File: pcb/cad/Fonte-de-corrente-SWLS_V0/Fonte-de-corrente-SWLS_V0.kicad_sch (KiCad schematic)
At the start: 31 parts, among them J2 LEMO FFA.0S, J3 LEMO FFA.0S, J4 Barrel_Jack_Switch, SW1 SW_DIP_x01, U1 LM7805, U2 LT3080xST, U3 LT3092xST, U4 LT3092xST, U5 74AHC1G04, U6 TS5A21366, U7 TS5A21366, U8 TS5A21366, U9 TS5A21366

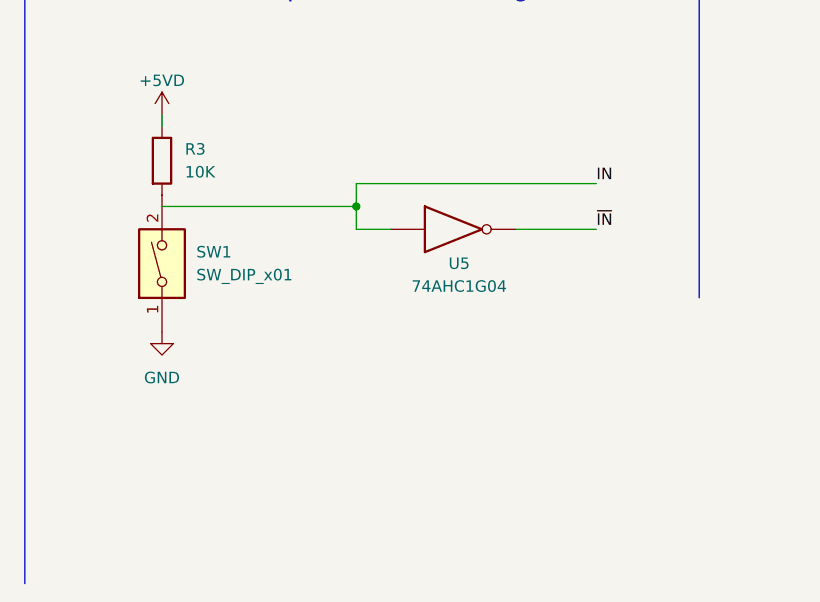
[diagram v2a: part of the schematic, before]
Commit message: Atualização do circuito esquemático, adição de footprints nod componentes
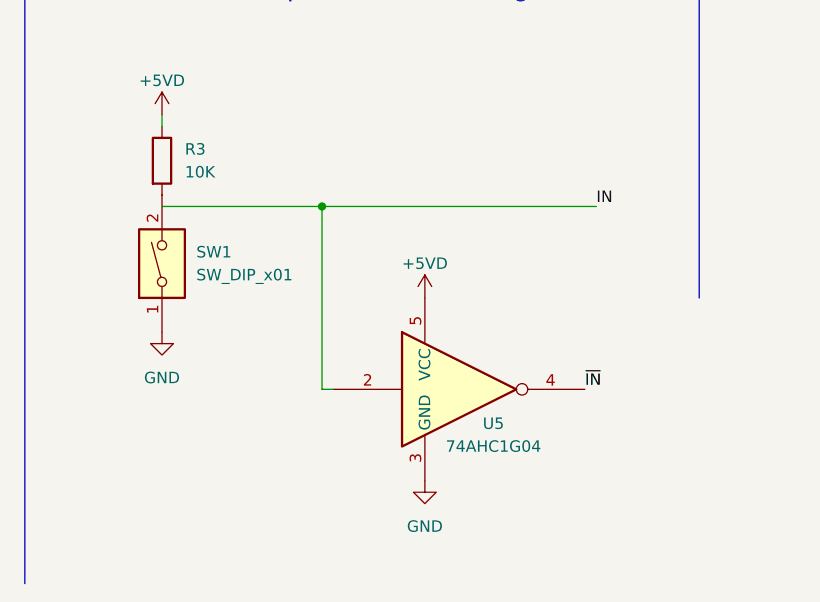
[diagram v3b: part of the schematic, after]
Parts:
- SW1: footprint (none) -> Button_Switch_THT:SW_DIP_SPSTx01_Piano_10.8x4.1mm_W7.62mm_P2.54mm; Numero do Produto (none) -> 418117270901
- U1: footprint (none) -> Package_TO_SOT_THT:TO-220-3_Vertical; Numero do produto (none) -> LM7805
- U5: footprint (none) -> Package_TO_SOT_SMD:SOT-353_SC-70-5_Handsoldering; Numero do produto (none) -> 74AHC1G04SE
- U6, U7, U8, U9: footprint (none) -> Package_SO:VSSOP-8_2.4x2.1mm_P0.5mm; Numero do produto (none) -> TS5A21366
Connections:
- net VCC is gone; now on net +5V: U5.5 (VCC)
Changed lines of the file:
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@@
   (junction (at 46.99 176.53) (diameter 0) (color 0 0 0 0)
   )
-  (junction (at 138.43 156.21) (diameter 0) (color 0 0 0 0)
-  )
   (junction (at 59.69 176.53) (diameter 0) (color 0 0 0 0)
   )
@@
   (junction (at 50.8 49.53) (diameter 0) (color 0 0 0 0)
   )
+  (junction (at 134.62 156.21) (diameter 0) (color 0 0 0 0)
+  )
   (junction (at 151.13 46.99) (diameter 0) (color 0 0 0 0)
   )
   (junction (at 46.99 46.99) (diameter 0) (color 0 0 0 0)
   )
-  (wire (pts (xy 138.43 158.75) (xy 142.24 158.75))
+  (wire (pts (xy 134.62 176.53) (xy 135.89 176.53))
     (stroke (width 0) (type default))
   )
@@
     (stroke (width 0) (type default))
   )
-  (wire (pts (xy 138.43 153.67) (xy 138.43 156.21))
-    (stroke (width 0) (type default))
-  )
   (wire (pts (xy 55.88 149.86) (xy 66.04 149.86))
     (stroke (width 0) (type default))
@@
     (stroke (width 0) (type default))
   )
-  (wire (pts (xy 116.84 156.21) (xy 138.43 156.21))
+  (wire (pts (xy 116.84 156.21) (xy 134.62 156.21))
     (stroke (width 0) (type default))
   )
@@
     (stroke (width 0) (type default))
   )
-  (wire (pts (xy 156.21 158.75) (xy 165.1 158.75))
-    (stroke (width 0) (type default))
-  )
   (wire (pts (xy 69.85 87.63) (xy 72.39 87.63))
     (stroke (width 0) (type default))
   )
-  (wire (pts (xy 138.43 153.67) (xy 165.1 153.67))
+  (wire (pts (xy 134.62 156.21) (xy 165.1 156.21))
     (stroke (width 0) (type default))
   )
@@
     (stroke (width 0) (type default))
   )
-  (wire (pts (xy 138.43 156.21) (xy 138.43 158.75))
+  (wire (pts (xy 134.62 156.21) (xy 134.62 176.53))
     (stroke (width 0) (type default))
   )
@@
     (effects (font (size 1.27 1.27)) (justify right bottom))
   )
-  (label "~{IN}" (at 165.1 158.75 0) (fields_autoplaced)
+  (label "~{IN}" (at 163.83 176.53 0) (fields_autoplaced)
     (effects (font (size 1.27 1.27)) (justify left bottom))
   )
@@
     (effects (font (size 1.27 1.27)) (justify right bottom))
   )
-  (label "IN" (at 165.1 153.67 0) (fields_autoplaced)
+  (label "IN" (at 165.1 156.21 0) (fields_autoplaced)
     (effects (font (size 1.27 1.27)) (justify left bottom))
   )
@@
       (effects (font (size 1.27 1.27)) (justify left))
     )
-    (property "Footprint" "" (at 259.08 90.17 0)
+    (property "Footprint" "Package_SO:VSSOP-8_2.4x2.1mm_P0.5mm" (at 259.08 90.17 0)
       (effects (font (size 1.27 1.27) italic) hide)
     )
-    (property "Datasheet" "" (at 259.08 90.17 0)
+    (property "Datasheet" "https://pdf1.alldatasheet.com/datasheet-pdf/view/346107/TI/TS5A21366.html" (at 259.08 90.17 0)
+      (effects (font (size 1.27 1.27)) hide)
+    )
+    (property "Numero do produto" "TS5A21366" (at 259.08 90.17 0)
       (effects (font (size 1.27 1.27)) hide)
     )
@@
     )
   )
-  (symbol (lib_id "74xGxx:74AHC1G04") (at 149.86 158.75 0) (unit 1)
-    (in_bom yes) (on_board yes) (dnp no)
-    (property "Reference" "U5" (at 149.86 162.56 0)
-      (effects (font (size 1.27 1.27)))
-    )
-    (property "Value" "74AHC1G04" (at 149.86 165.1 0)
-      (effects (font (size 1.27 1.27)))
-    )
-    (property "Footprint" "" (at 149.86 158.75 0)
-      (effects (font (size 1.27 1.27)) hide)
-    )
-    (property "Datasheet" "http://www.ti.com/lit/sg/scyt129e/scyt129e.pdf" (at 149.86 158.75 0)
+  (symbol (lib_id "74xGxx:74AHC1G04") (at 151.13 176.53 0) (unit 1)
+    (in_bom yes) (on_board yes) (dnp no)
+    (property "Reference" "U5" (at 153.67 180.34 0)
+      (effects (font (size 1.27 1.27)))
+    )
+    (property "Value" "74AHC1G04" (at 153.67 182.88 0)
+      (effects (font (size 1.27 1.27)))
+    )
+    (property "Footprint" "Package_TO_SOT_SMD:SOT-353_SC-70-5_Handsoldering" (at 151.13 176.53 0)
+      (effects (font (size 1.27 1.27)) hide)
+    )
+    (property "Datasheet" "http://www.ti.com/lit/sg/scyt129e/scyt129e.pdf" (at 151.13 176.53 0)
+      (effects (font (size 1.27 1.27)) hide)
+    )
+    (property "Numero do produto" "74AHC1G04SE" (at 151.13 176.53 0)
       (effects (font (size 1.27 1.27)) hide)
     )
@@
       (effects (font (size 1.27 1.27)))
     )
-    (property "Footprint" "" (at 55.88 136.525 0)
+    (property "Footprint" "Package_TO_SOT_THT:TO-220-3_Vertical" (at 55.88 136.525 0)
       (effects (font (size 1.27 1.27) italic) hide)
     )
-    (property "Datasheet" "" (at 55.88 143.51 0)
+    (property "Datasheet" "https://www.sparkfun.com/datasheets/Components/LM7805.pdf" (at 55.88 143.51 0)
+      (effects (font (size 1.27 1.27)) hide)
+    )
+    (property "Numero do produto" "LM7805" (at 55.88 142.24 0)
       (effects (font (size 1.27 1.27)) hide)
     )
@@
       (effects (font (size 1.27 1.27)) (justify left))
     )
-    (property "Footprint" "" (at 257.81 41.91 0)
+    (property "Footprint" "Package_SO:VSSOP-8_2.4x2.1mm_P0.5mm" (at 257.81 41.91 0)
       (effects (font (size 1.27 1.27) italic) hide)
     )
-    (property "Datasheet" "" (at 257.81 41.91 0)
+    (property "Datasheet" "https://pdf1.alldatasheet.com/datasheet-pdf/view/346107/TI/TS5A21366.html" (at 257.81 41.91 0)
+      (effects (font (size 1.27 1.27)) hide)
+    )
+    (property "Numero do produto" "TS5A21366" (at 257.81 41.91 0)
       (effects (font (size 1.27 1.27)) hide)
     )
@@
       (effects (font (size 1.27 1.27)) (justify left))
     )
-    (property "Footprint" "" (at 209.55 90.17 0)
+    (property "Footprint" "Package_SO:VSSOP-8_2.4x2.1mm_P0.5mm" (at 209.55 90.17 0)
       (effects (font (size 1.27 1.27) italic) hide)
     )
-    (property "Datasheet" "" (at 209.55 90.17 0)
+    (property "Datasheet" "https://pdf1.alldatasheet.com/datasheet-pdf/view/346107/TI/TS5A21366.html" (at 209.55 90.17 0)
+      (effects (font (size 1.27 1.27)) hide)
+    )
+    (property "Numero do produto" "TS5A21366" (at 209.55 90.17 0)
       (effects (font (size 1.27 1.27)) hide)
     )
@@
       (effects (font (size 1.27 1.27)) (justify left))
     )
-    (property "Footprint" "" (at 212.09 40.64 0)
+    (property "Footprint" "Package_SO:VSSOP-8_2.4x2.1mm_P0.5mm" (at 212.09 40.64 0)
       (effects (font (size 1.27 1.27) italic) hide)
     )
-    (property "Datasheet" "" (at 212.09 40.64 0)
+    (property "Datasheet" "https://pdf1.alldatasheet.com/datasheet-pdf/view/346107/TI/TS5A21366.html" (at 212.09 40.64 0)
+      (effects (font (size 1.27 1.27)) hide)
+    )
+    (property "Numero do produto" "TS5A21366" (at 212.09 40.64 0)
       (effects (font (size 1.27 1.27)) hide)
     )
@@
     )
   )
+  (symbol (lib_name "GND_2") (lib_id "power:GND") (at 146.05 186.69 0) (unit 1)
+    (in_bom yes) (on_board yes) (dnp no) (fields_autoplaced)
+    (property "Reference" "#PWR025" (at 146.05 193.04 0)
+      (effects (font (size 1.27 1.27)) hide)
+    )
+    (property "Value" "GND" (at 146.05 191.77 0)
+      (effects (font (size 1.27 1.27)))
+    )
+    (property "Footprint" "" (at 146.05 186.69 0)
+      (effects (font (size 1.27 1.27)) hide)
+    )
+    (property "Datasheet" "" (at 146.05 186.69 0)
+      (effects (font (size 1.27 1.27)) hide)
+    )
+    (pin "1")
+    (instances
+      (project "Fonte-de-corrente-SWLS_V0"
+        (path "/485d57e1-9e59-4bdb-b543-f102996c1764"
+          (reference "#PWR025") (unit 1)
+        )
+      )
+    )
+  )
   (symbol (lib_name "GND_2") (lib_id "power:GND") (at 257.81 62.23 0) (unit 1)
     (in_bom yes) (on_board yes) (dnp no) (fields_autoplaced)
@@
         (path "/485d57e1-9e59-4bdb-b543-f102996c1764"
           (reference "C5") (unit 1)
+        )
+      )
+    )
+  )
+  (symbol (lib_id "power:+5VD") (at 146.05 166.37 0) (unit 1)
+    (in_bom yes) (on_board yes) (dnp no)
+    (property "Reference" "#PWR026" (at 146.05 170.18 0)
+      (effects (font (size 1.27 1.27)) hide)
+    )
+    (property "Value" "+5VD" (at 146.05 162.56 0)
+      (effects (font (size 1.27 1.27)))
+    )
+    (property "Footprint" "" (at 146.05 166.37 0)
+      (effects (font (size 1.27 1.27)) hide)
+    )
+    (property "Datasheet" "" (at 146.05 166.37 0)
+      (effects (font (size 1.27 1.27)) hide)
+    )
+    (pin "1")
+    (instances
+      (project "Fonte-de-corrente-SWLS_V0"
+        (path "/485d57e1-9e59-4bdb-b543-f102996c1764"
+          (reference "#PWR026") (unit 1)
         )
       )
@@
       (effects (font (size 1.27 1.27)) (justify right))
     )
-    (property "Footprint" "" (at 116.84 162.56 0)
-      (effects (font (size 1.27 1.27)) hide)
-    )
-    (property "Datasheet" "~" (at 116.84 162.56 0)
-      (effects (font (size 1.27 1.27)) hide)
-    )
+    (property "Footprint" "Button_Switch_THT:SW_DIP_SPSTx01_Piano_10.8x4.1mm_W7.62mm_P2.54mm" (at 116.84 162.56 0)
+      (effects (font (size 1.27 1.27)) hide)
+    )
+    (property "Datasheet" "https://br.mouser.com/datasheet/2/445/418117270901-3086928.pdf" (at 116.84 162.56 0)
+      (effects (font (size 1.27 1.27)) hide)
+    )
+    (property "Numero do Produto" "418117270901" (at 116.84 162.56 90)
+      (effects (font (size 1.27 1.27)) hide)
+    )

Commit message: Incio do placement de fonte de corrente
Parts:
- C2, C3, C4, C6, C7, C8, C9: footprint (none) -> Capacitor_SMD:C_0805_2012Metric
- J2, J3: footprint (none) -> Fonte-de-corrente-SWLS-complementar:Lemo_Painel_4vias
- R3: footprint (none) -> Resistor_SMD:R_0805_2012Metric
- U1: footprint Package_TO_SOT_THT:TO-220-3_Vertical -> Package_TO_SOT_THT:TO-92
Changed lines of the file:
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@@
       (effects (font (size 1.27 1.27)) (justify left))
     )
-    (property "Footprint" "" (at 67.0052 149.86 0)
+    (property "Footprint" "Capacitor_SMD:C_0805_2012Metric" (at 67.0052 149.86 0)
       (effects (font (size 1.27 1.27)) hide)
     )
@@
       (effects (font (size 1.27 1.27)) (justify left))
     )
-    (property "Footprint" "" (at 45.4152 149.86 0)
+    (property "Footprint" "Capacitor_SMD:C_0805_2012Metric" (at 45.4152 149.86 0)
       (effects (font (size 1.27 1.27)) hide)
     )
@@
       (effects (font (size 1.27 1.27)))
     )
-    (property "Footprint" "" (at 259.08 146.05 0)
+    (property "Footprint" "Fonte-de-corrente-SWLS-complementar:Lemo_Painel_4vias" (at 259.08 146.05 0)
       (effects (font (size 1.27 1.27)) hide)
     )
@@
       (effects (font (size 1.27 1.27)) (justify left))
     )
-    (property "Footprint" "" (at 55.5752 49.53 0)
+    (property "Footprint" "Capacitor_SMD:C_0805_2012Metric" (at 55.5752 49.53 0)
       (effects (font (size 1.27 1.27)) hide)
     )
@@
       (effects (font (size 1.27 1.27)))
     )
-    (property "Footprint" "Package_TO_SOT_THT:TO-220-3_Vertical" (at 55.88 136.525 0)
+    (property "Footprint" "Package_TO_SOT_THT:TO-92" (at 55.88 136.525 0)
       (effects (font (size 1.27 1.27) italic) hide)
     )
@@
       (effects (font (size 1.27 1.27)))
     )
-    (property "Footprint" "" (at 214.63 146.05 0)
+    (property "Footprint" "Fonte-de-corrente-SWLS-complementar:Lemo_Painel_4vias" (at 214.63 146.05 0)
       (effects (font (size 1.27 1.27)) hide)
     )
@@
       (effects (font (size 1.27 1.27)) (justify left))
     )
-    (property "Footprint" "" (at 115.062 151.13 90)
+    (property "Footprint" "Resistor_SMD:R_0805_2012Metric" (at 115.062 151.13 90)
       (effects (font (size 1.27 1.27)) hide)
     )
@@
       (effects (font (size 1.27 1.27)) (justify left))
     )
-    (property "Footprint" "" (at 47.9552 184.15 0)
+    (property "Footprint" "Capacitor_SMD:C_0805_2012Metric" (at 47.9552 184.15 0)
       (effects (font (size 1.27 1.27)) hide)
     )
@@
       (effects (font (size 1.27 1.27)) (justify left))
     )
-    (property "Footprint" "" (at 73.3552 184.15 0)
+    (property "Footprint" "Capacitor_SMD:C_0805_2012Metric" (at 73.3552 184.15 0)
       (effects (font (size 1.27 1.27)) hide)
     )
@@
       (effects (font (size 1.27 1.27)) (justify left))
     )
-    (property "Footprint" "" (at 60.6552 184.15 0)
+    (property "Footprint" "Capacitor_SMD:C_0805_2012Metric" (at 60.6552 184.15 0)
       (effects (font (size 1.27 1.27)) hide)
     )
@@
       (effects (font (size 1.27 1.27)) (justify left))
     )
-    (property "Footprint" "" (at 35.2552 184.15 0)
-      (effects (font (size 1.27 1.27)) hide)
-    )
+    (property "Footprint" "Capacitor_SMD:C_0805_2012Metric" (at 35.2552 184.15 0)
+      (effects (font (size 1.27 1.27)) hide)
+    )

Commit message: Atualização do layout da PCB
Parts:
- added C10: 0.1uF, Capacitor_SMD:C_0805_2012Metric, symbol Device:C
- R1, R2: value 1MR -> 1M
- R4, R5: value 100R -> 100
- R6, R7: value 22KR -> 22K
- R8, R9: value 120R -> 120
- SW1: footprint Button_Switch_THT:SW_DIP_SPSTx01_Piano_10.8x4.1mm_W7.62mm_P2.54mm -> Fonte-de-corrente-SWLS-complementar:Chave analógica
- U1: value LM7805 -> LM78L05
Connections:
- net +5V: now also C10.1
- net GND: now also C10.2
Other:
- note added: "R_{OUT}"
- note added: "R_{SET}"
- moved on the sheet: U5
